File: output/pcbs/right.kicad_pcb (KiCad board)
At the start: 2 copper layers, 137 x 116.2 mm, 79 parts

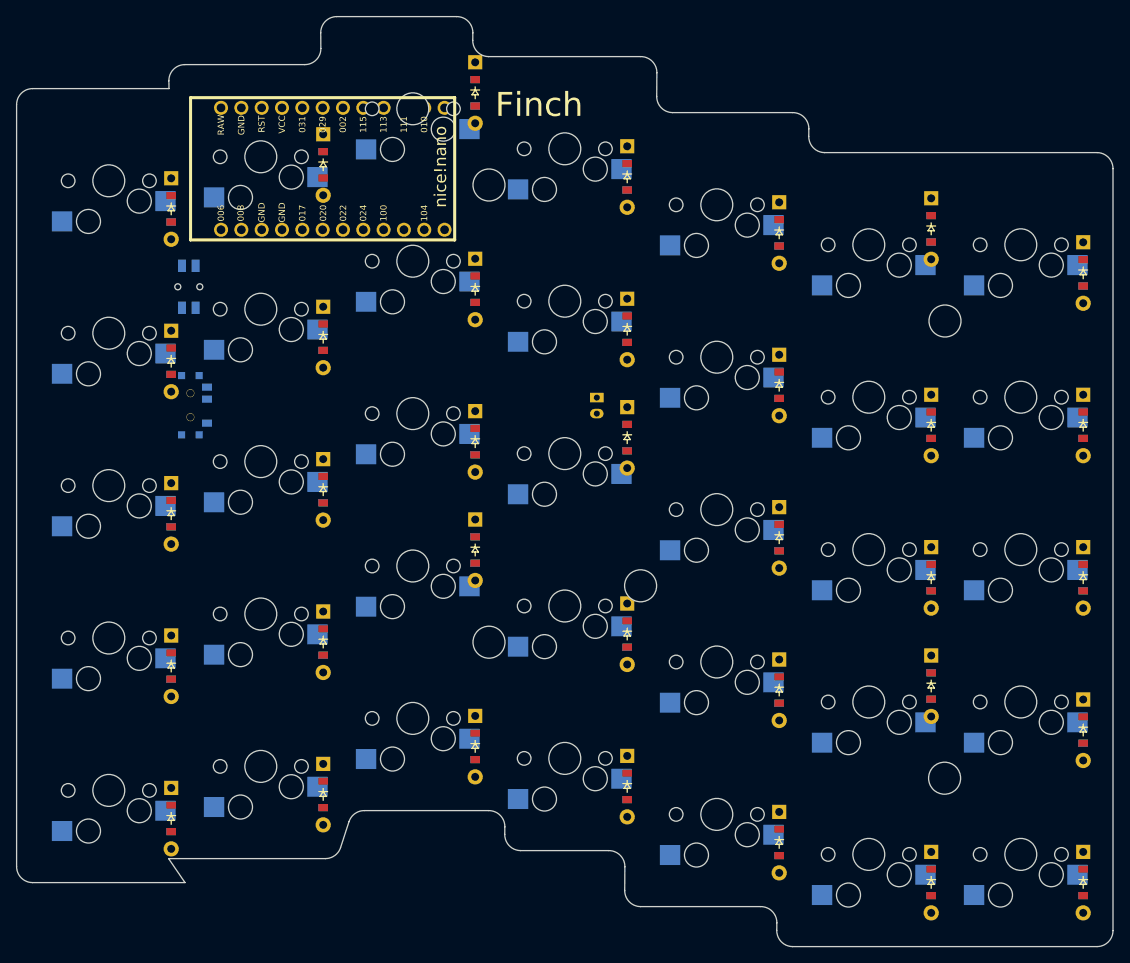
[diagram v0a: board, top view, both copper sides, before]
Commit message: updated diode pos., controller, and outlines
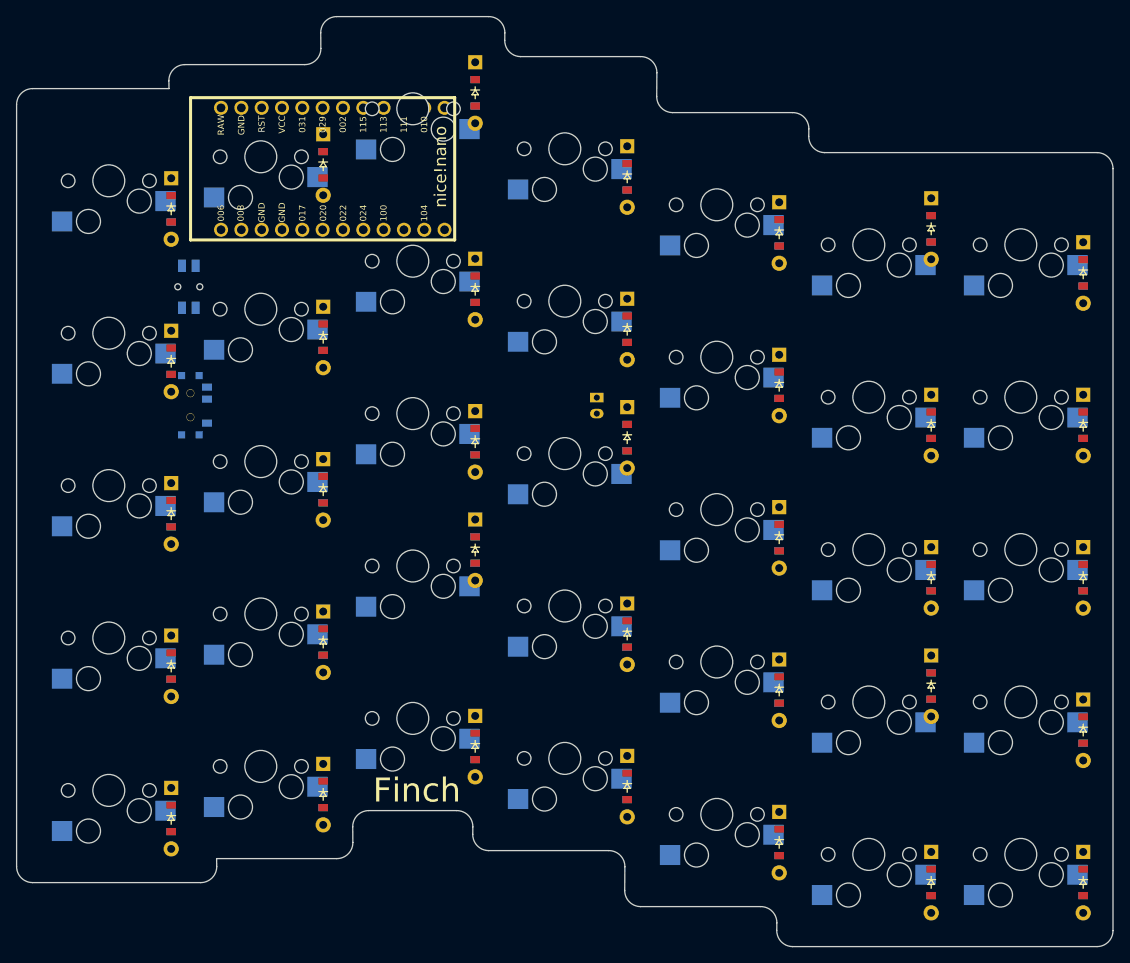
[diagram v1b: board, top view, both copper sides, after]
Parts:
- removed ? (x5): , HOLE_M2_TH
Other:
- outline, holes or cut-outs redrawn
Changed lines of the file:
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@@
             (pad "" smd rect (at -3.7 -1.1 90) (size 0.9 0.9) (layers B.Cu B.Paste B.Mask))
         )
-    (module HOLE_M2_TH (layer F.Cu)
-      (at 321.525 123.475 0)
-      (pad "" np_thru_hole circle (at 0 0 90) (size 4.0 4.0) (drill 4.0) (layers *.Cu *.Mask F.SilkS) (clearance 0.3)))
-    (module HOLE_M2_TH (layer F.Cu)
-      (at 378.475 140.475 0)
-      (pad "" np_thru_hole circle (at 0 0 90) (size 4.0 4.0) (drill 4.0) (layers *.Cu *.Mask F.SilkS) (clearance 0.3)))
-    (module HOLE_M2_TH (layer F.Cu)
-      (at 378.525 83.325 0)
-      (pad "" np_thru_hole circle (at 0 0 90) (size 4.0 4.0) (drill 4.0) (layers *.Cu *.Mask F.SilkS) (clearance 0.3)))
-    (module HOLE_M2_TH (layer F.Cu)
-      (at 321.525 66.325 0)
-      (pad "" np_thru_hole circle (at 0 0 90) (size 4.0 4.0) (drill 4.0) (layers *.Cu *.Mask F.SilkS) (clearance 0.3)))
-    (module HOLE_M2_TH (layer F.Cu)
-      (at 340.475 116.425 0)
-      (pad "" np_thru_hole circle (at 0 0 90) (size 4.0 4.0) (drill 4.0) (layers *.Cu *.Mask F.SilkS) (clearance 0.3)))
-            (gr_text "Finch" (at 322.3 56.30000000000001 0) (layer F.SilkS)
-                (effects (font (size 3 3) (thickness 0.4) ) (justify left))
+            (gr_text "Finch" (at 318 142 0) (layer F.SilkS)
+                (effects (font (size 3 3) (thickness 0.4) ) (justify right))
             )
   (gr_line (start 399.525 159.525) (end 399.525 64.275) (angle 90) (layer Edge.Cuts) (width 0.15))
@@
 (gr_line (start 359.50490001000003 57.27500000000001) (end 344.4893367521429 57.27500000000001) (angle 90) (layer Edge.Cuts) (width 0.15))
 (gr_line (start 342.48938775285717 55.26071460000094) (end 342.51061224714294 52.28928539998742) (angle 90) (layer Edge.Cuts) (width 0.15))
-(gr_line (start 340.5106632478571 50.27500000000001) (end 321.49509999 50.27500000000001) (angle 90) (layer Edge.Cuts) (width 0.15))
-(gr_line (start 319.49519999 48.255001000004995) (end 319.50480001 47.29499900000519) (angle 90) (layer Edge.Cuts) (width 0.15))
-(gr_line (start 317.50490001 45.27500000000001) (end 302.49170246278675 45.27500000000001) (angle 90) (layer Edge.Cuts) (width 0.15))
+(gr_line (start 340.5106632478571 50.27500000000001) (end 325.49509999 50.27500000000001) (angle 90) (layer Edge.Cuts) (width 0.15))
+(gr_line (start 323.49519999 48.255001000004995) (end 323.50480001 47.29499900000155) (angle 90) (layer Edge.Cuts) (width 0.15))
+(gr_line (start 321.50490001 45.27500000000001) (end 302.49170246278675 45.27500000000001) (angle 90) (layer Edge.Cuts) (width 0.15))
 (gr_line (start 300.4917716627867 47.291632799999206) (end 300.50812833721335 49.258367200003704) (angle 90) (layer Edge.Cuts) (width 0.15))
 (gr_line (start 298.50819753721333 51.27500000000001) (end 283.5086111116667 51.27500000000001) (angle 90) (layer Edge.Cuts) (width 0.15))
@@
 (gr_line (start 281.525 54.27500000000001) (end 264.475 54.27500000000001) (angle 90) (layer Edge.Cuts) (width 0.15))
 (gr_line (start 262.475 56.27500000000001) (end 262.475 151.525) (angle 90) (layer Edge.Cuts) (width 0.15))
-(gr_line (start 264.475 153.525) (end 283.525 153.525) (angle 90) (layer Edge.Cuts) (width 0.15))
-(gr_line (start 283.525 153.525) (end 281.475 150.525) (angle 90) (layer Edge.Cuts) (width 0.15))
-(gr_line (start 281.475 150.525) (end 301.0720259675 150.525) (angle 90) (layer Edge.Cuts) (width 0.15))
-(gr_line (start 302.9740940476583 149.14317216105133) (end 304.02590595234176 145.9068278389484) (angle 90) (layer Edge.Cuts) (width 0.15))
-(gr_line (start 305.92797403250006 144.525) (end 321.50490001 144.525) (angle 90) (layer Edge.Cuts) (width 0.15))
-(gr_line (start 323.50480001 146.54499899999792) (end 323.49519999 147.50500099999772) (angle 90) (layer Edge.Cuts) (width 0.15))
-(gr_line (start 325.49509999 149.525) (end 336.5106632478571 149.525) (angle 90) (layer Edge.Cuts) (width 0.15))
+(gr_line (start 264.475 153.525) (end 285.49138888833335 153.525) (angle 90) (layer Edge.Cuts) (width 0.15))
+(gr_line (start 287.49111118663933 151.4916711983642) (end 287.475 150.525) (angle 90) (layer Edge.Cuts) (width 0.15))
+(gr_line (start 287.475 150.525) (end 302.50826384916667 150.525) (angle 90) (layer Edge.Cuts) (width 0.15))
+(gr_line (start 304.50819444999985 148.508333999991) (end 304.49180555000004 146.5416660000119) (angle 90) (layer Edge.Cuts) (width 0.15))
+(gr_line (start 306.49173615083333 144.525) (end 317.50490001 144.525) (angle 90) (layer Edge.Cuts) (width 0.15))
+(gr_line (start 319.50480001 146.54499899999792) (end 319.49519998999995 147.505001000005) (angle 90) (layer Edge.Cuts) (width 0.15))
+(gr_line (start 321.49509999 149.525) (end 336.5106632478571 149.525) (angle 90) (layer Edge.Cuts) (width 0.15))
 (gr_line (start 338.51061224714294 151.53928539998742) (end 338.4893877528571 154.5107146000082) (angle 90) (layer Edge.Cuts) (width 0.15))
 (gr_line (start 340.4893367521429 156.525) (end 355.5049000099999 156.525) (angle 90) (layer Edge.Cuts) (width 0.15))
@@
 (gr_arc (start 344.4893367521429 55.27500000000001) (end 342.4893877521429 55.260714600000014) (angle -90.40925004051249) (layer Edge.Cuts) (width 0.15))
 (gr_arc (start 340.5106632478571 52.275000000001455) (end 342.5106122478571 52.289285400001454) (angle -90.4092500401369) (layer Edge.Cuts) (width 0.15))
-(gr_arc (start 321.49509999 48.27500000000001) (end 319.49519999 48.255001000000014) (angle -90.57293869754076) (layer Edge.Cuts) (width 0.15))
-(gr_arc (start 317.50490001 47.275000000001455) (end 319.50480001 47.294999000001454) (angle -90.5729386977905) (layer Edge.Cuts) (width 0.15))
+(gr_arc (start 325.49509999 48.27500000000001) (end 323.49519999 48.255001000000014) (angle -90.57293869754076) (layer Edge.Cuts) (width 0.15))
+(gr_arc (start 321.50490001 47.275000000001455) (end 323.50480001 47.294999000001454) (angle -90.57293869768625) (layer Edge.Cuts) (width 0.15))
 (gr_arc (start 302.49170246278675 47.27500000000001) (end 302.49170246278675 45.27500000000001) (angle -90.47650012213157) (layer Edge.Cuts) (width 0.15))
 (gr_arc (start 298.50819753721333 49.275000000001455) (end 298.50819753721333 51.275000000001455) (angle -90.47650012209024) (layer Edge.Cuts) (width 0.15))
@@
 (gr_arc (start 264.475 56.27500000000001) (end 264.475 54.27500000000001) (angle -90) (layer Edge.Cuts) (width 0.15))
 (gr_arc (start 264.475 151.525) (end 262.475 151.525) (angle -90) (layer Edge.Cuts) (width 0.15))
-(gr_arc (start 301.0720259675 148.525) (end 301.0720259675 150.525) (angle -71.99583744051091) (layer Edge.Cuts) (width 0.15))
-(gr_arc (start 305.92797403250006 146.52499999999986) (end 305.92797403250006 144.52499999999986) (angle -71.99583744050705) (layer Edge.Cuts) (width 0.15))
-(gr_arc (start 321.50490001 146.525) (end 323.50480001 146.54499900000002) (angle -90.5729386976235) (layer Edge.Cuts) (width 0.15))
-(gr_arc (start 325.49509999 147.52499999999782) (end 323.49519999 147.5050009999978) (angle -90.57293869768628) (layer Edge.Cuts) (width 0.15))
+(gr_arc (start 285.49138888833335 151.525) (end 285.49138888833335 153.525) (angle -90.9548440227083) (layer Edge.Cuts) (width 0.15))
+(gr_arc (start 302.50826384916667 148.525) (end 302.50826384916667 150.525) (angle -90.47745124689271) (layer Edge.Cuts) (width 0.15))
+(gr_arc (start 306.49173615083333 146.52500000000146) (end 306.49173615083333 144.52500000000146) (angle -90.47745124693421) (layer Edge.Cuts) (width 0.15))
+(gr_arc (start 317.50490001 146.525) (end 319.50480001 146.54499900000002) (angle -90.5729386976235) (layer Edge.Cuts) (width 0.15))
+(gr_arc (start 321.49509999 147.52500000000146) (end 319.49519999 147.50500100000144) (angle -90.57293869758206) (layer Edge.Cuts) (width 0.15))
 (gr_arc (start 336.5106632478571 151.525) (end 338.5106122478571 151.5392854) (angle -90.40925004017845) (layer Edge.Cuts) (width 0.15))
 (gr_arc (start 340.4893367521429 154.52500000000146) (end 338.4893877521429 154.51071460000145) (angle -90.4092500403454) (layer Edge.Cuts) (width 0.15))

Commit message: Updated diode pos and controller pos on right hand
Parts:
- moved D31 112.7 mm to (274.0, 118.0), turned to 0 degrees
- moved D30 103.1 mm to (274.0, 137.0), turned to 0 degrees
- moved D25 98.4 mm to (312.0, 51.8), turned to 0 degrees
- moved D32 64.8 mm to (274.0, 98.9), turned to 0 degrees
- moved D9 61.7 mm to (369.0, 87.8), turned to 0 degrees
- moved D10 61.7 mm to (369.0, 68.8), turned to 0 degrees
- moved D14 59.7 mm to (350.0, 82.9), turned to 0 degrees
- moved D15 59.7 mm to (350.0, 63.8), turned to 0 degrees
- moved D33 55.9 mm to (274.0, 79.9), turned to 0 degrees
- moved D16 49.3 mm to (331.0, 133.0), turned to 0 degrees
- moved D17 49.3 mm to (331.0, 114.0), turned to 0 degrees
- moved D34 46.2 mm to (274.0, 60.8), turned to 0 degrees
- moved D18 43.1 mm to (331.0, 94.9), turned to 0 degrees
- moved D11 30.6 mm to (350.0, 140.0), turned to 0 degrees
- moved D12 30.6 mm to (350.0, 121.0), turned to 0 degrees
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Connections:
- D10 pad 1: P20 -> P15
- D10 pad 2: mirror_third_bottom -> mirror_second_num
- D11 pad 1: P19 -> P21
- D11 pad 2: mirror_third_home -> mirror_third_mod
- D12 pad 1: P18 -> P20
- D12 pad 2: mirror_third_top -> mirror_third_bottom
- D13 pad 1: P15 -> P19
- D13 pad 2: mirror_third_num -> mirror_third_home
- D14 pad 1: P21 -> P18
- D14 pad 2: mirror_fourth_mod -> mirror_third_top
- D15 pad 1: P20 -> P15
- D15 pad 2: mirror_fourth_bottom -> mirror_third_num
- D16 pad 1: P18 -> P21
- D16 pad 2: mirror_fourth_top -> mirror_fourth_mod
- D17 pad 1: P15 -> P20
- D17 pad 2: mirror_fourth_num -> mirror_fourth_bottom
- D18 pad 1: P21 -> P19
- D18 pad 2: mirror_fifth_mod -> mirror_fourth_home
- D19 pad 1: P19 -> P18
- D19 pad 2: mirror_fifth_home -> mirror_fourth_top
- D20 pad 1: P18 -> P15
- D20 pad 2: mirror_fifth_top -> mirror_fourth_num
- D21 pad 2: mirror_sixth_mod -> mirror_fifth_mod
- D22 pad 2: mirror_sixth_bottom -> mirror_fifth_bottom
- D23 pad 2: mirror_sixth_home -> mirror_fifth_home
- D24 pad 2: mirror_sixth_top -> mirror_fifth_top
- D25 pad 1: P21 -> P15
- D25 pad 2: mirror_seventh_mod -> mirror_fifth_num
- D26 pad 1: P20 -> P21
- D26 pad 2: mirror_seventh_bottom -> mirror_sixth_mod
- D27 pad 1: P19 -> P20
- D27 pad 2: mirror_seventh_home -> mirror_sixth_bottom
- D28 pad 1: P18 -> P19
- D28 pad 2: mirror_seventh_top -> mirror_sixth_home
- D29 pad 1: P15 -> P18
- D29 pad 2: mirror_seventh_num -> mirror_sixth_top
- D30 pad 1: P20 -> P21
- D30 pad 2: mirror_second_bottom -> mirror_seventh_mod
- D31 pad 1: P15 -> P20
- D31 pad 2: mirror_second_num -> mirror_seventh_bottom
- D32 pad 2: mirror_fourth_home -> mirror_seventh_home
- D33 pad 1: P20 -> P18
- D33 pad 2: mirror_fifth_bottom -> mirror_seventh_top
- D34 pad 2: mirror_fifth_num -> mirror_seventh_num
- D7 pad 1: P19 -> P20
- D7 pad 2: mirror_second_home -> mirror_second_bottom
- D8 pad 1: P18 -> P19
- D8 pad 2: mirror_second_top -> mirror_second_home
- D9 pad 1: P21 -> P18
- D9 pad 2: mirror_third_mod -> mirror_second_top
